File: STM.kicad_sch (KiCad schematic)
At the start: 0 parts

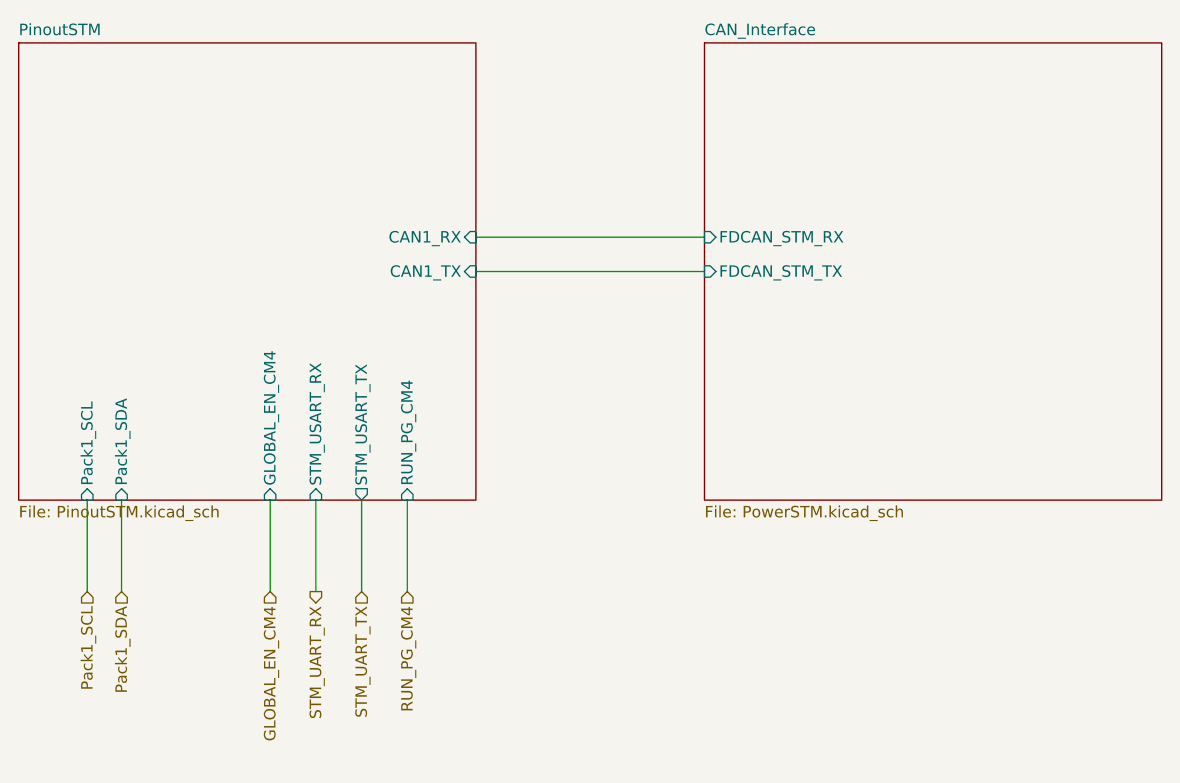
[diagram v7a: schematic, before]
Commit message: added some testpoints
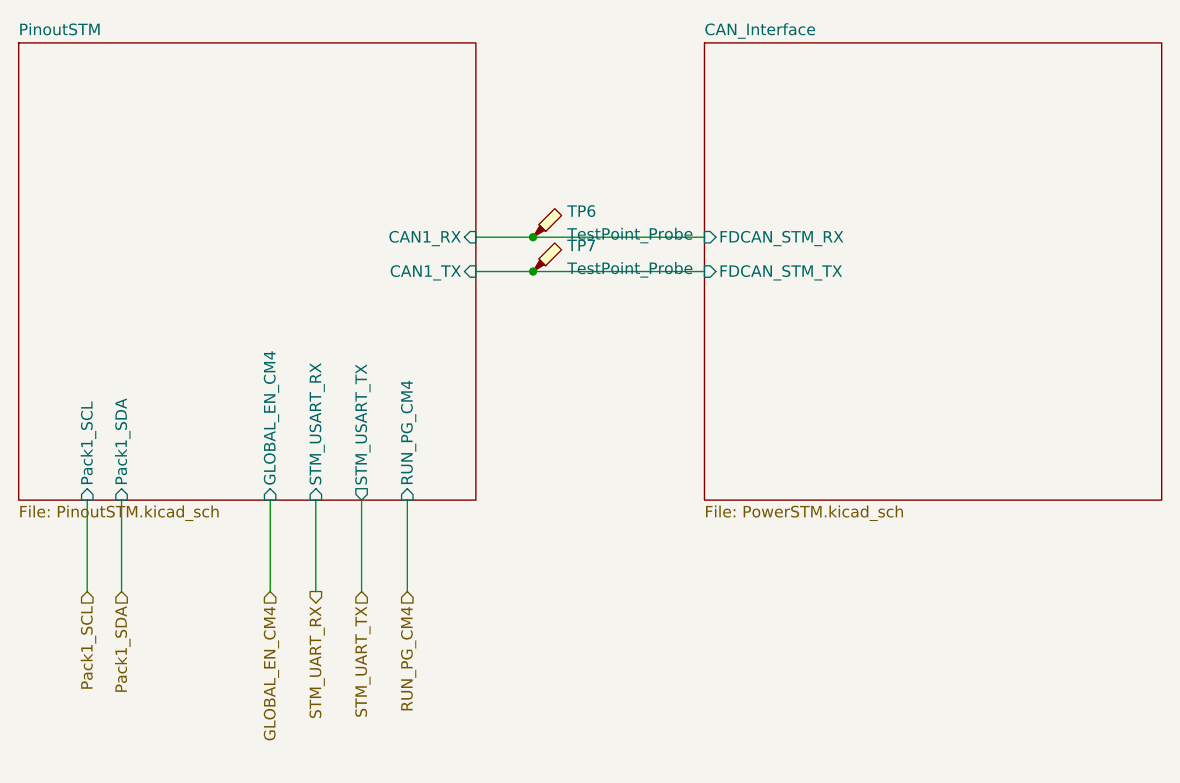
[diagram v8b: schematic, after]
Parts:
- added TP6, TP7: TestPoint_Probe, TestPoint:TestPoint_THTPad_D2.5mm_Drill1.2mm, symbol Connector:TestPoint_Probe
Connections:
- net CAN_Interface/FDCAN_STM_RX: now also TP6.1
- net CAN_Interface/FDCAN_STM_TX: now also TP7.1
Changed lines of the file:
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@@
 	(generator_version "9.0")
 	(paper "A4")
-	(wire
-		(pts
-			(xy 76.2 46.99) (xy 101.6 46.99)
+	(junction
+		(at 82.55 50.8)
+		(diameter 0)
+		(color 0 0 0 0)
+	)
+	(junction
+		(at 82.55 46.99)
+		(diameter 0)
+		(color 0 0 0 0)
+	)
+	(wire
+		(pts
+			(xy 76.2 46.99) (xy 82.55 46.99)
 		)
 		(stroke
@@
 	(wire
 		(pts
-			(xy 76.2 50.8) (xy 101.6 50.8)
+			(xy 76.2 50.8) (xy 82.55 50.8)
+		)
+		(stroke
+			(width 0)
+			(type default)
+		)
+	)
+	(wire
+		(pts
+			(xy 82.55 46.99) (xy 101.6 46.99)
 		)
 		(stroke
@@
 		(pts
 			(xy 58.42 76.2) (xy 58.42 86.36)
+		)
+		(stroke
+			(width 0)
+			(type default)
+		)
+	)
+	(wire
+		(pts
+			(xy 82.55 50.8) (xy 101.6 50.8)
 		)
 		(stroke
@@
 		)
 	)
+	(symbol
+		(lib_id "Connector:TestPoint_Probe")
+		(at 82.55 46.99 0)
+		(unit 1)
+		(exclude_from_sim no)
+		(in_bom yes)
+		(on_board yes)
+		(dnp no)
+		(fields_autoplaced yes)
+		(property "Reference" "TP6"
+			(at 86.36 44.1324 0)
+			(effects
+				(font
+					(size 1.27 1.27)
+				)
+				(justify left)
+			)
+		)
+		(property "Value" "TestPoint_Probe"
+			(at 86.36 46.6724 0)
+			(effects
+				(font
+					(size 1.27 1.27)
+				)
+				(justify left)
+			)
+		)
+		(property "Footprint" "TestPoint:TestPoint_THTPad_D2.5mm_Drill1.2mm"
+			(at 87.63 46.99 0)
+			(effects
+				(font
+					(size 1.27 1.27)
+				)
+				(hide yes)
+			)
+		)
+		(property "Datasheet" "~"
+			(at 87.63 46.99 0)
+			(effects
+				(font
+					(size 1.27 1.27)
+				)
+				(hide yes)
+			)
+		)
+		(property "Description" "test point (alternative probe-style design)"
+			(at 82.55 46.99 0)
+			(effects
+				(font
+					(size 1.27 1.27)
+				)
+				(hide yes)
+			)
+		)
+		(pin "1"
+		)
+		(instances
+			(project "nautilus_mainboard"
+				(path "/ce1819b2-f280-40ed-834f-6fe4d12f809d/46fb4fb5-44f2-465b-b1ff-e4e0fbef74ae"
+					(reference "TP6")
+					(unit 1)
+				)
+			)
+		)
+	)
+	(symbol
+		(lib_id "Connector:TestPoint_Probe")
+		(at 82.55 50.8 0)
+		(unit 1)
+		(exclude_from_sim no)
+		(in_bom yes)
+		(on_board yes)
+		(dnp no)
+		(fields_autoplaced yes)
+		(property "Reference" "TP7"
+			(at 86.36 47.9424 0)
+			(effects
+				(font
+					(size 1.27 1.27)
+				)
+				(justify left)
+			)
+		)
+		(property "Value" "TestPoint_Probe"
+			(at 86.36 50.4824 0)
+			(effects
+				(font
+					(size 1.27 1.27)
+				)
+				(justify left)
+			)
+		)
+		(property "Footprint" "TestPoint:TestPoint_THTPad_D2.5mm_Drill1.2mm"
+			(at 87.63 50.8 0)
+			(effects
+				(font
+					(size 1.27 1.27)
+				)
+				(hide yes)
+			)
+		)
+		(property "Datasheet" "~"
+			(at 87.63 50.8 0)
+			(effects
+				(font
+					(size 1.27 1.27)
+				)
+				(hide yes)
+			)
+		)
+		(property "Description" "test point (alternative probe-style design)"
+			(at 82.55 50.8 0)
+			(effects
+				(font
+					(size 1.27 1.27)
+				)
+				(hide yes)
+			)
+		)
+		(pin "1"
+		)
+		(instances
+			(project "nautilus_mainboard"
+				(path "/ce1819b2-f280-40ed-834f-6fe4d12f809d/46fb4fb5-44f2-465b-b1ff-e4e0fbef74ae"
+					(reference "TP7")
+					(unit 1)
+				)
+			)
+		)
+	)
